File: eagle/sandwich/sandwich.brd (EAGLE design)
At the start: 100 x 81.3 mm, 120 parts, among them IC1 ATMEGA644-20PU, J1 AVR_SPI_PRG_6NS, Q1 20MHZ, Q2 MOSFET-NCHANNELFQP30N06L, Q3 MOSFET-NCHANNELFQP30N06L, T0 47k, T1 47k, T2 47k, T3 47k

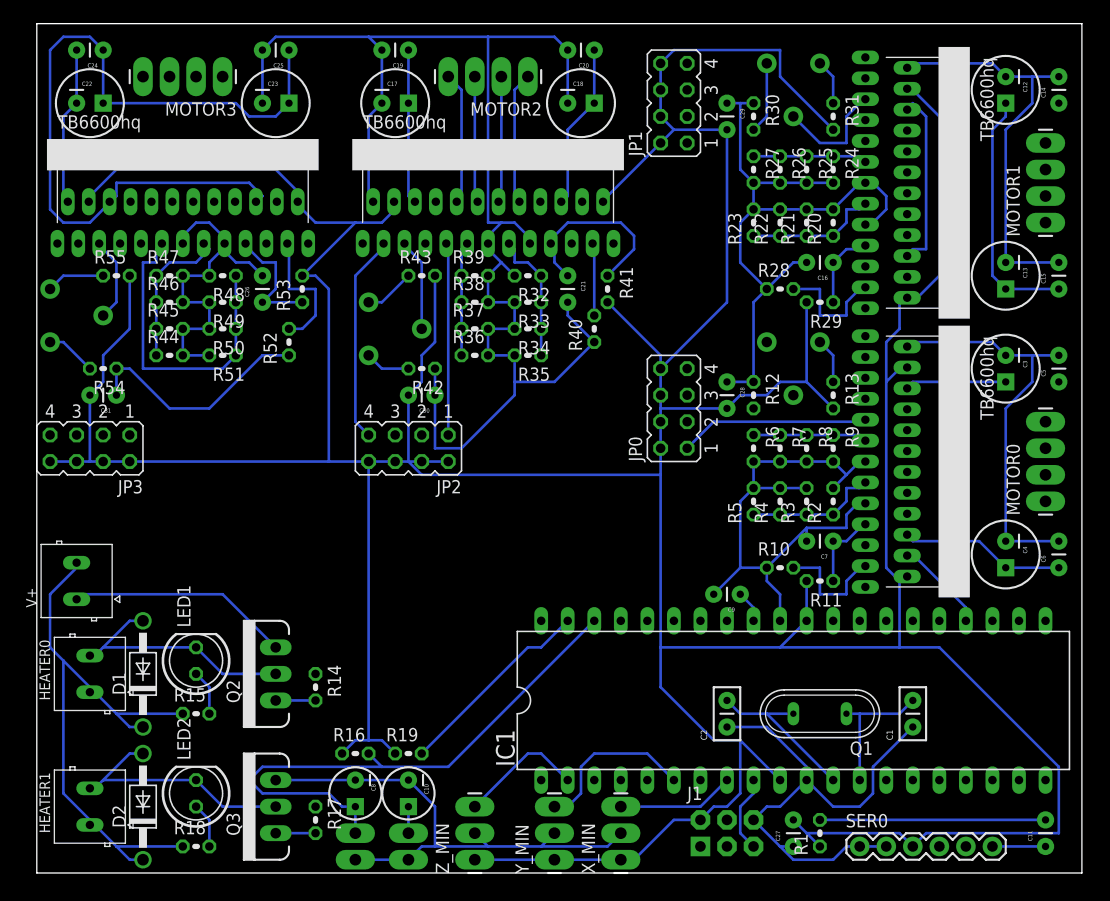
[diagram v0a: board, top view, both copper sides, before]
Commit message: Changed motor connectors back to screw terminals, added a fan output and routed the board layout.
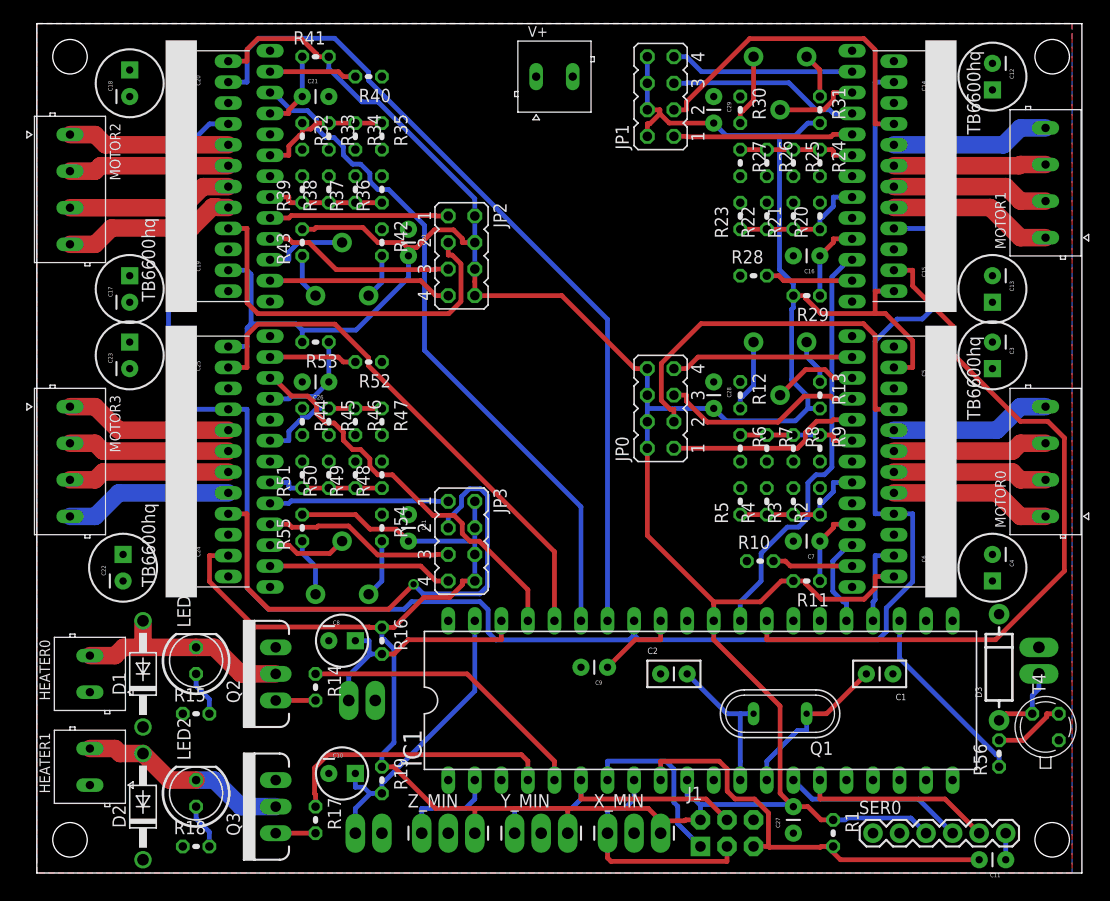
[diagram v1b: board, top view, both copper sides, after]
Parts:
- added D3: (no value), SparkFun-DiscreteSemi:DIODE-1N4001
- added FAN: (no value), SparkFun-Connectors:1X02_LONGPADS
- added R56: (no value), resistor:0204V
- added T4: 2N2222, transistor:TO18
- added U$5, U$6, U$7, U$8: (no value), SparkFun-Electromechanical:STAND-OFF
- MOTOR0, MOTOR1, MOTOR2, MOTOR3: value (none) -> DG3XX-04-3.5; device SparkFun-Connectors:1X04_LONGPADS -> degson:DG350-3.5-04P
- moved V+ 66.5 mm to (49.5, 76.2), turned to 0 degrees
- moved C24 47.6 mm to (14.0, 31.8), turned to 270 degrees
- moved MOTOR2 45.1 mm to (3.17, 65.4), turned to 270 degrees
- moved C22 44.6 mm to (8.26, 29.2), turned to 90 degrees
- moved C18 43.2 mm to (8.89, 75.6), turned to 90 degrees
- moved MOTOR3 39.6 mm to (3.17, 39.4), turned to 270 degrees
- moved C20 39.4 mm to (14.0, 76.8), turned to 270 degrees
- moved T3 38.6 mm to (29.2, 26.7), turned to 90 degrees
- moved JP3 36.7 mm to (40.6, 31.8), turned to 270 degrees
- moved R41 35.7 mm to (26.7, 78.1), turned to 0 degrees
- moved R40 32.4 mm to (31.8, 76.2), turned to 180 degrees
- moved C17 31.0 mm to (8.89, 55.9), turned to 90 degrees
- moved C25 30.9 mm to (14.0, 49.5), turned to 270 degrees
- moved R54 30.7 mm to (33.0, 33.0), turned to 270 degrees
- moved C21 30.6 mm to (25.4, 74.3), turned to 0 degrees
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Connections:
- removed net AUX7: IC1.23
- new net FAN: IC1.23, R56.1
- new net N$26: D3.A, FAN.2, T4.3
- new net N$73: R56.2, T4.2
- net +5V: now also X_MIN.3, Y_MIN.3, Z_MIN.3; no longer X_MIN.1, Y_MIN.1, Z_MIN.1
- net GND: now also T4.1, TEMP0.2, TEMP1.2; no longer TEMP0.1, TEMP1.1
- net MOSI: now also Y_MIN.1; no longer Y_MIN.3
- net SCK: now also X_MIN.1; no longer X_MIN.3
- net TEMP0: now also TEMP0.1; no longer TEMP0.2
- net TEMP1: now also TEMP1.1; no longer TEMP1.2
- net V+: now also D3.C, FAN.1
- net Z_MIN: now also Z_MIN.1; no longer Z_MIN.3
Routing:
- net GND: track 528.9 -> 0.00 mm
- net V+: track 245.5 -> 0.00 mm
- net ENABLE: track 0.00 -> 173.5 mm
- net +5V: track 525.2 -> 436.2 mm
- net DIR2: track 0.00 -> 80.3 mm
- net DIR1: track 0.00 -> 71.1 mm
- net STEP2: track 0.00 -> 65.5 mm
- net DIR3: track 0.00 -> 50.8 mm
- net N$69: track 0.00 -> 49.9 mm, vias 0 -> 1
- net STEP1: track 0.00 -> 40.3 mm
- net STEP3: track 0.00 -> 38.0 mm
- net N$22: track 0.00 -> 37.7 mm
- net N$54: track 0.00 -> 36.7 mm
- net TEMP0: track 54.9 -> 22.9 mm
- net N$39: track 0.00 -> 31.8 mm
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- added copper zone on layer 16, net GND
- added copper zone on layer 1, net V+

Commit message: Changed trim pots to 4.7k
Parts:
- T0, T1, T2, T3: value 47k -> 4.7k
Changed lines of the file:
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@@
 <element name="C7" library="SparkFun-Capacitors" package="CAP-PTH-SMALL" value="0.1uF" x="74.93" y="31.75" rot="R180"/>
 <element name="R11" library="resistor" package="0204V" value="4.7k" x="73.66" y="27.94" rot="R180"/>
-<element name="T0" library="SparkFun-Electromechanical" package="TRIM_POT" value="47k" x="71.12" y="50.8" rot="R270"/>
+<element name="T0" library="SparkFun-Electromechanical" package="TRIM_POT" value="4.7k" x="71.12" y="50.8" rot="R270"/>
 <element name="R12" library="resistor" package="0204V" value="1k" x="67.31" y="45.72" rot="R270"/>
 <element name="R13" library="resistor" package="0204V" value="1k" x="74.93" y="45.72" rot="R270"/>
@@
 <element name="C16" library="SparkFun-Capacitors" package="CAP-PTH-SMALL" value="0.1uF" x="74.93" y="59.055" rot="R180"/>
 <element name="R29" library="resistor" package="0204V" value="4.7k" x="73.66" y="55.245" rot="R180"/>
-<element name="T1" library="SparkFun-Electromechanical" package="TRIM_POT" value="47k" x="71.12" y="78.105" rot="R270"/>
+<element name="T1" library="SparkFun-Electromechanical" package="TRIM_POT" value="4.7k" x="71.12" y="78.105" rot="R270"/>
 <element name="R30" library="resistor" package="0204V" value="1k" x="67.31" y="73.025" rot="R270"/>
 <element name="R31" library="resistor" package="0204V" value="1k" x="74.93" y="73.025" rot="R270"/>
@@
 <element name="C21" library="SparkFun-Capacitors" package="CAP-PTH-SMALL" value="0.1uF" x="25.4" y="74.295"/>
 <element name="R41" library="resistor" package="0204V" value="4.7k" x="26.67" y="78.105"/>
-<element name="T2" library="SparkFun-Electromechanical" package="TRIM_POT" value="47k" x="29.21" y="55.245" rot="R90"/>
+<element name="T2" library="SparkFun-Electromechanical" package="TRIM_POT" value="4.7k" x="29.21" y="55.245" rot="R90"/>
 <element name="R42" library="resistor" package="0204V" value="1k" x="33.02" y="60.325" rot="R270"/>
 <element name="R43" library="resistor" package="0204V" value="1k" x="25.4" y="60.325" rot="R90"/>
@@
 <element name="C26" library="SparkFun-Capacitors" package="CAP-PTH-SMALL" value="0.1uF" x="27.94" y="46.99" rot="R180"/>
 <element name="R53" library="resistor" package="0204V" value="4.7k" x="26.67" y="50.8" rot="R180"/>
-<element name="T3" library="SparkFun-Electromechanical" package="TRIM_POT" value="47k" x="29.21" y="26.67" rot="R90"/>
+<element name="T3" library="SparkFun-Electromechanical" package="TRIM_POT" value="4.7k" x="29.21" y="26.67" rot="R90"/>
 <element name="R54" library="resistor" package="0204V" value="1k" x="33.02" y="33.02" rot="R270"/>
 <element name="R55" library="resistor" package="0204V" value="1k" x="25.4" y="33.02" rot="R90"/>

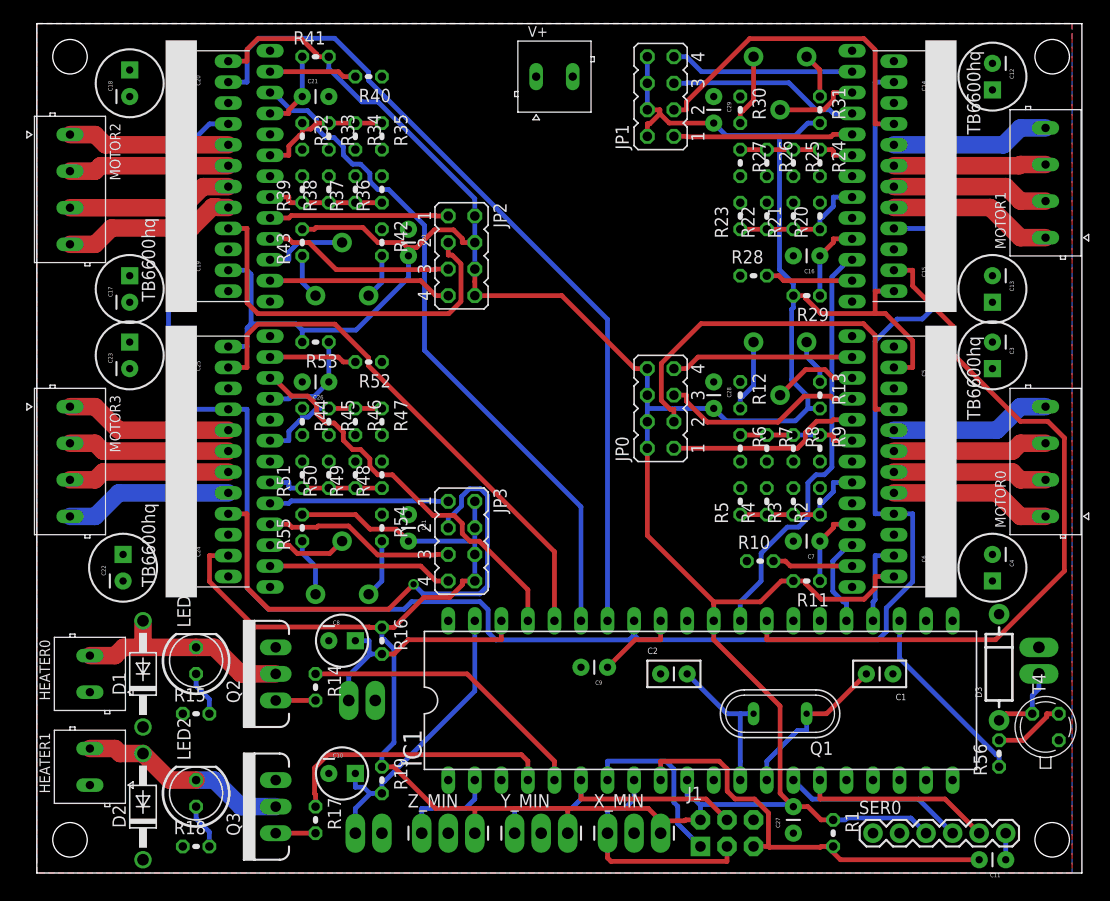
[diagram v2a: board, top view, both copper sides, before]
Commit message: This seems like a millable layout and routing
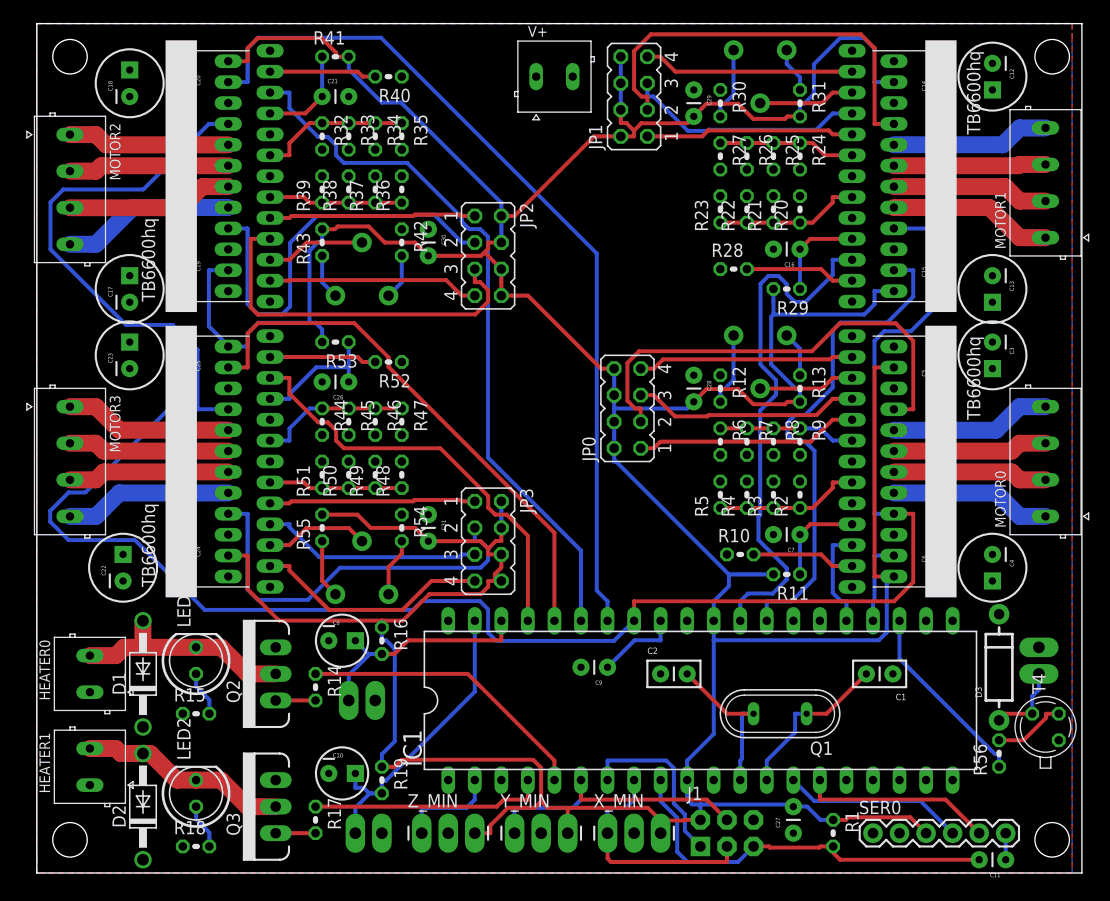
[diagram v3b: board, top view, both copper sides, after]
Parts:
- moved JP0 3.17 mm to (56.5, 44.5)
- moved JP1 2.54 mm to (57.1, 74.3)
- moved JP2 2.54 mm to (43.2, 59.1)
- moved JP3 2.54 mm to (43.2, 31.8)
- moved R24 2.01 mm to (73.0, 68.6)
- moved R25 2.01 mm to (70.5, 68.6)
- moved R26 2.01 mm to (67.9, 68.6)
- moved R27 2.01 mm to (65.4, 68.6)
- moved R29 2.01 mm to (71.8, 55.9)
- moved T0 2.01 mm to (69.2, 51.4)
- moved R10 2.01 mm to (67.3, 30.5)
- moved C16 2.01 mm to (73.0, 59.7)
- moved C7 2.01 mm to (73.0, 32.4)
- moved R11 2.01 mm to (71.8, 28.6)
- moved R12 2.01 mm to (65.4, 46.4)
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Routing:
- net ENABLE: track 173.5 -> 210.0 mm
- net +5V: track 436.2 -> 458.9 mm
- net DIR1: track 71.1 -> 48.5 mm
- net N$55: track 18.3 -> 35.9 mm
- net N$69: track 49.9 -> 38.0 mm, vias 1 -> 0
- net STEP1: track 40.3 -> 51.0 mm
- net N$39: track 31.8 -> 39.8 mm
- net N$22: track 37.7 -> 44.5 mm
- net N$71: track 17.6 -> 22.7 mm
- net N$40: track 18.3 -> 22.9 mm
- net HEATER1: track 26.7 -> 22.5 mm
- net N$54: track 36.7 -> 39.9 mm
- net STEP2: track 65.5 -> 68.7 mm
- net N$24: track 17.5 -> 20.7 mm
- net STEP3: track 38.0 -> 41.1 mm
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
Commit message: Updated TB6600 package, moved R56, changed 100uF caps to 16v, disabled GND and V+ thermals. Still needs TB6600HG layout adjustment and new routing
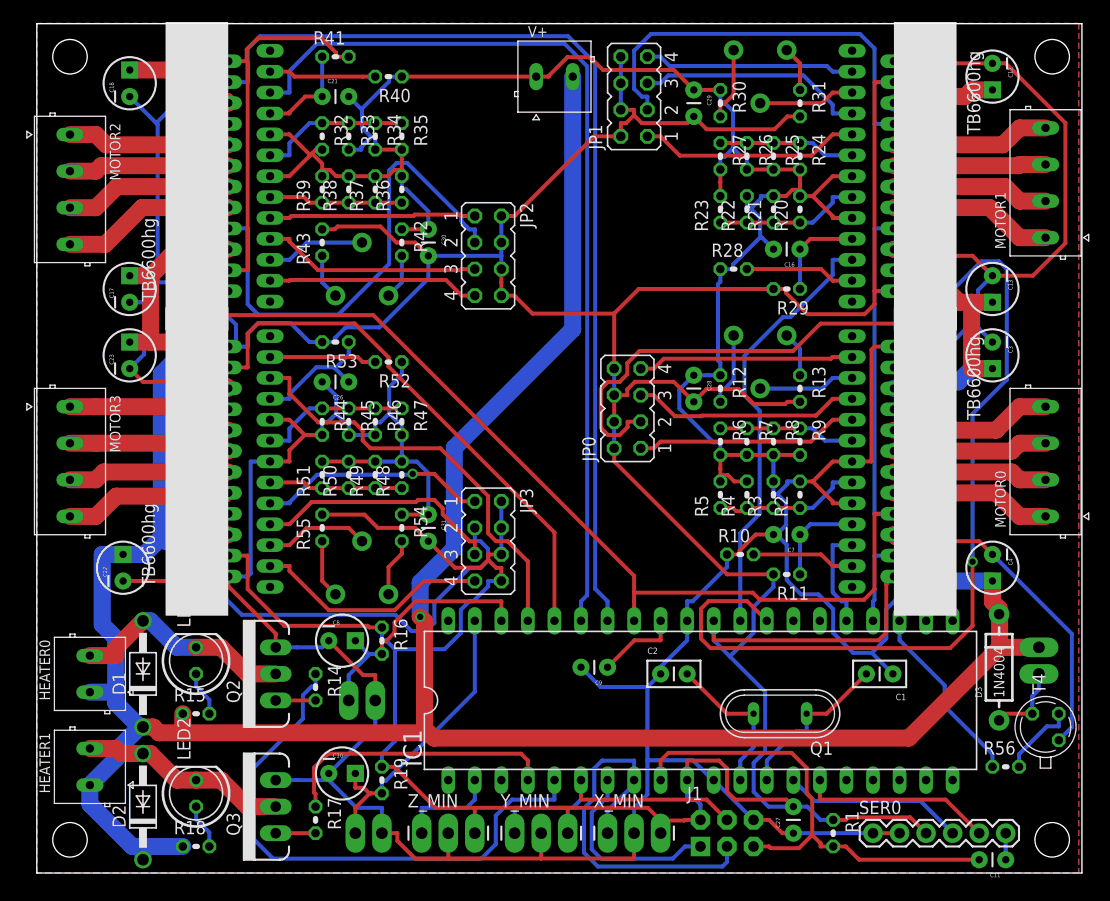
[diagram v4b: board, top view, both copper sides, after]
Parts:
- C12, C13, C17, C18, C22, C23, C3, C4: device SparkFun-Passives:CPOL-RADIAL-100UF-25V -> SparkFun-Passives:CPOL-RADIAL-10UF-25V
- D3: value (none) -> 1N4004
- R56: value (none) -> 1k7
- U$1, U$2, U$3, U$4: value TB6600HQ -> TB6600HG; device tb6600hq:TB6600HQ -> tb6600hq:P-HZIP25-1.00G
- moved R56 1.42 mm to (92.7, 10.2), turned to 0 degrees
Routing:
- net GND: track 0.00 -> 620.5 mm
- net V+: track 0.00 -> 382.2 mm, vias 0 -> 1
- net ENABLE: track 210.0 -> 150.7 mm, vias 0 -> 1
- net DIR1: track 48.5 -> 86.9 mm, vias 0 -> 1
- net HEATER0: track 28.2 -> 53.8 mm
- net STEP2: track 68.7 -> 87.7 mm
- net +5V: track 458.9 -> 476.2 mm
- net N$55: track 35.9 -> 21.0 mm
- net SCK: track 22.6 -> 36.7 mm
- net N$22: track 44.5 -> 56.9 mm
- net DIR2: track 83.0 -> 93.7 mm
- net STEP1: track 51.0 -> 41.7 mm
- net RESET: track 38.6 -> 46.7 mm
- net N$69: track 38.0 -> 44.9 mm
- net N$54: track 39.9 -> 46.6 mm
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
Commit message: Adjusted layout for larger TB6600 package, routed with improved traces for V+ and GND
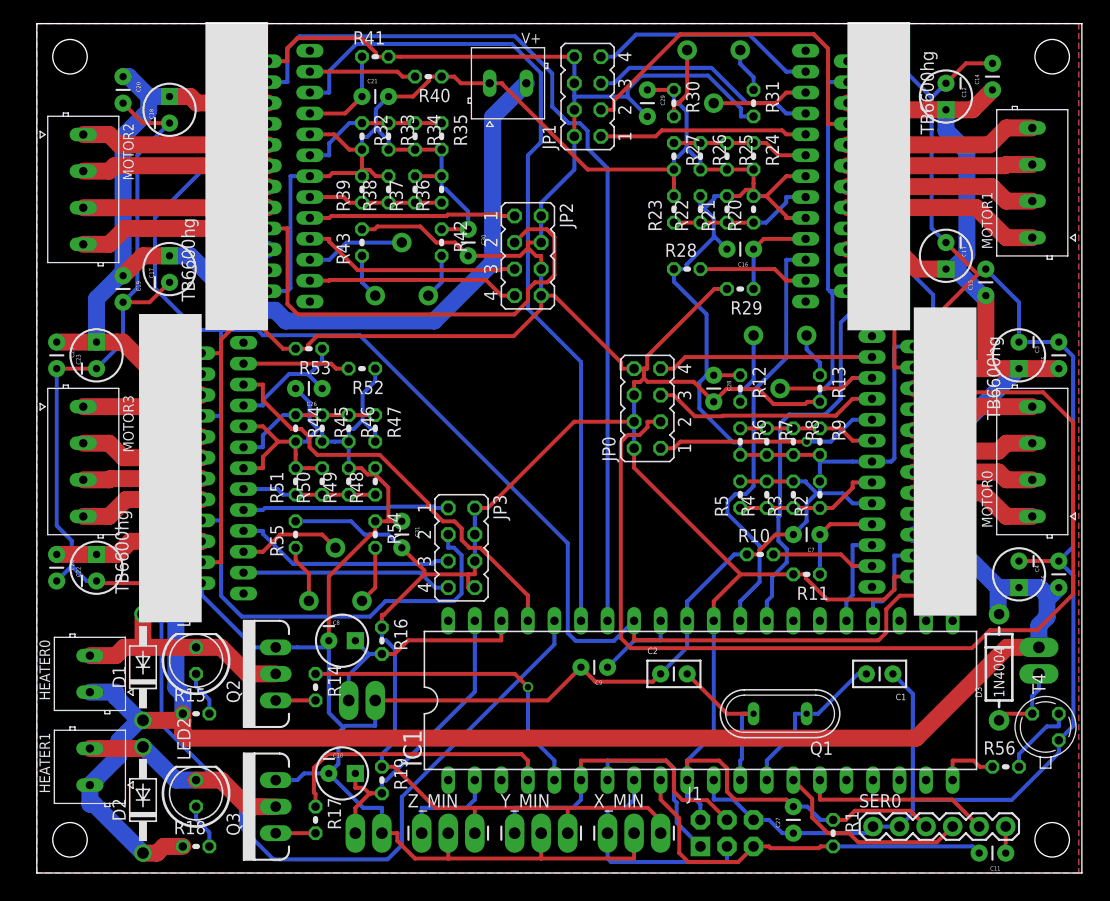
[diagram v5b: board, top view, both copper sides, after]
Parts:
- Q2, Q3: value MOSFET-NCHANNELFQP30N06L -> IRFZ44N
- moved C24 12.1 mm to (1.91, 30.5)
- moved C25 12.1 mm to (1.91, 50.8)
- moved C6 11.6 mm to (97.8, 27.3)
- moved C5 11.5 mm to (97.8, 48.3)
- moved C19 6.02 mm to (8.26, 57.1)
- moved C20 5.75 mm to (8.26, 76.2)
- moved C13 5.46 mm to (87.0, 59.1)
- moved C14 5.12 mm to (91.4, 74.9)
- moved C12 4.84 mm to (87.0, 74.3)
- moved C15 4.62 mm to (90.8, 55.2)
- moved C18 4.58 mm to (12.7, 73.0)
- moved V+ 4.49 mm to (45.1, 75.6)
- moved C16 4.45 mm to (68.6, 59.7)
- moved R20 4.45 mm to (68.6, 63.5)
- moved R24 4.45 mm to (68.6, 68.6)
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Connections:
- net AUX4: now also IC1.23; no longer IC1.20
- net FAN: now also IC1.20; no longer IC1.23
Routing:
- net N$22: track 56.9 -> 103.1 mm
- net DIR1: track 86.9 -> 42.0 mm, vias 1 -> 0
- net DIR3: track 52.1 -> 94.2 mm
- net GND: track 620.5 -> 648.3 mm
- net HEATER0: track 53.8 -> 30.8 mm, vias 0 -> 1
- net ENABLE: track 150.7 -> 173.2 mm, vias 1 -> 0
- net V+: track 382.2 -> 403.1 mm, vias 1 -> 0
- net +5V: track 476.2 -> 459.6 mm
- net SCK: track 36.7 -> 22.6 mm
- net FAN: track 17.7 -> 5.92 mm
- net RESET: track 46.7 -> 37.8 mm
- net STEP2: track 87.7 -> 81.4 mm
- net DIR2: track 93.7 -> 87.6 mm
- net N$39: track 39.8 -> 34.9 mm
- net N$69: track 44.9 -> 40.3 mm
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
